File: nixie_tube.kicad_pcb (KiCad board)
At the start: 2 copper layers, 25.8 x 56.3 mm, 28 parts, among them J1 Conn_01x06_Male, J11 dc003a, J2 Conn_01x06_Female, J3 Conn_01x01_Male, J4 Conn_01x01_Female, Q1 SS8550, Q2 FQD5N60C, Q3 Q_NPN_BCE, Q4 TP0610T, U1 MC34063

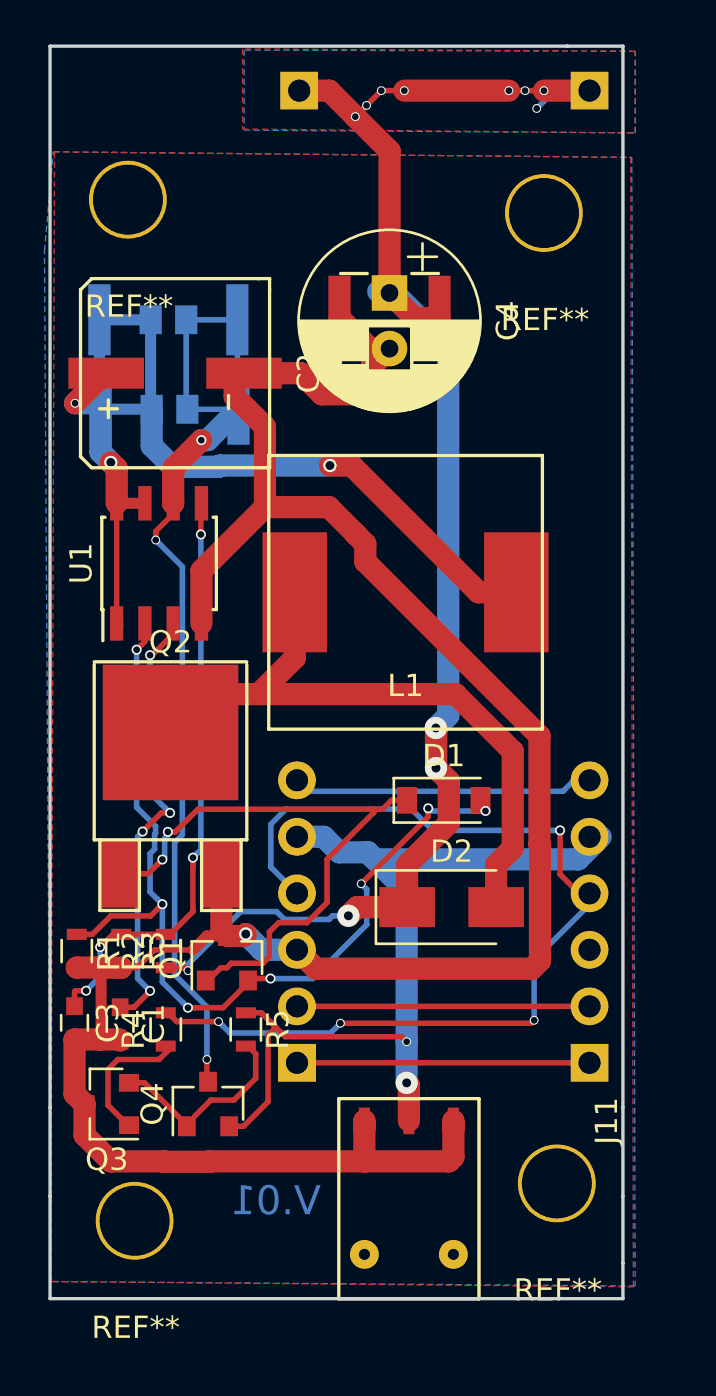
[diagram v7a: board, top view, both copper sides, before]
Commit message: extend ao3407 pad for making soldering easier when we dont want HV switching
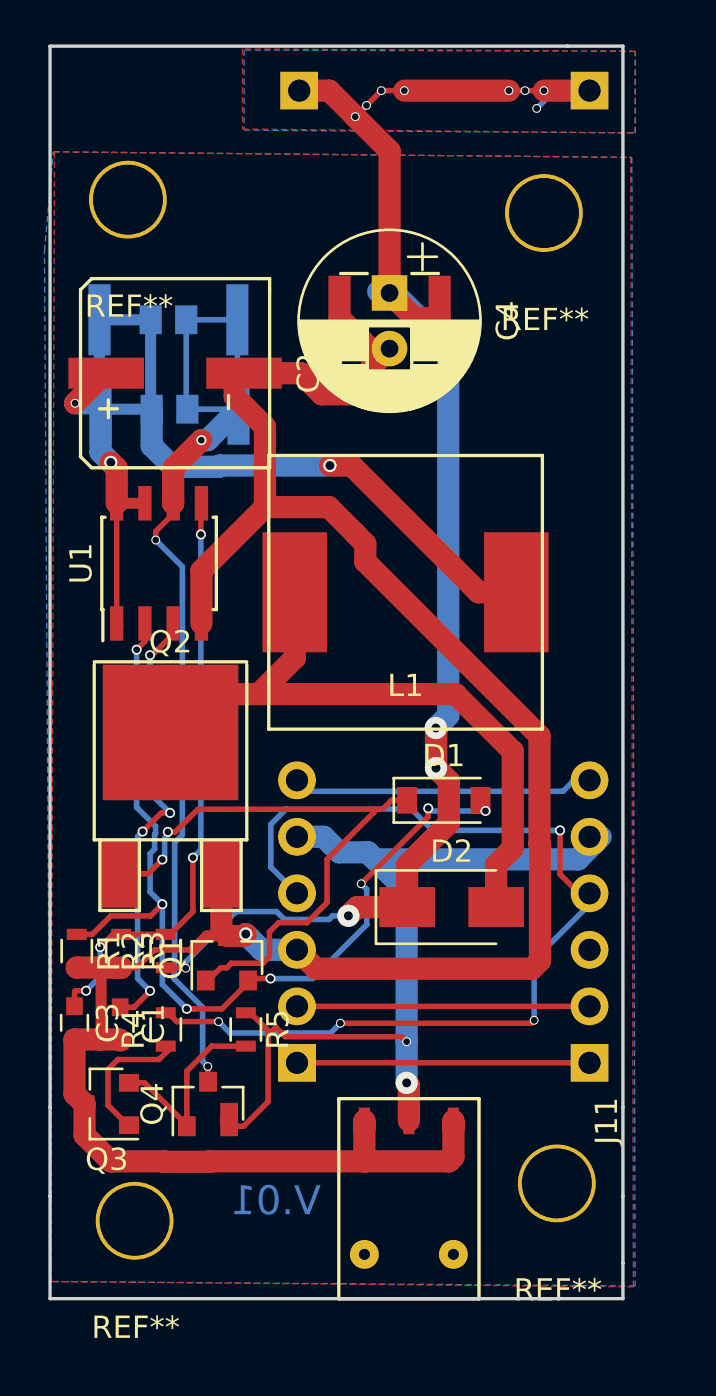
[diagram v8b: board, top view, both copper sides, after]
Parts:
- Q4: footprint TO_SOT_Packages_SMD:SOT-23 -> nixie-tube-fp:SOT-23-alt_solder_on2_3
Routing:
- net Net-(Q3-Pad2): track 8.48 -> 9.03 mm
